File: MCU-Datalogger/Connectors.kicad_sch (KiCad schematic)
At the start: 4 parts, among them J1 Conn_01x04_Pin, J2 Conn_01x04_Pin, J3 Conn_01x09_Pin, J4 Conn_02x03_Odd_Even

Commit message: Associate footprints with symbols
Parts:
- J1, J2: footprint (none) -> Connector_PinHeader_2.54mm:PinHeader_1x04_P2.54mm_Vertical
- J3: footprint (none) -> Connector_PinHeader_2.54mm:PinHeader_1x09_P2.54mm_Vertical
- J4: footprint (none) -> Connector_PinHeader_2.54mm:PinHeader_2x03_P2.54mm_Vertical
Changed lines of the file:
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@@
       (effects (font (size 1.27 1.27)))
     )
-    (property "Footprint" "" (at 143.51 86.36 0)
+    (property "Footprint" "Connector_PinHeader_2.54mm:PinHeader_1x04_P2.54mm_Vertical" (at 143.51 86.36 0)
       (effects (font (size 1.27 1.27)) hide)
     )
@@
       (effects (font (size 1.27 1.27)))
     )
-    (property "Footprint" "" (at 149.86 120.65 0)
+    (property "Footprint" "Connector_PinHeader_2.54mm:PinHeader_2x03_P2.54mm_Vertical" (at 149.86 120.65 0)
       (effects (font (size 1.27 1.27)) hide)
     )
@@
       (effects (font (size 1.27 1.27)))
     )
-    (property "Footprint" "" (at 121.92 120.65 0)
+    (property "Footprint" "Connector_PinHeader_2.54mm:PinHeader_1x09_P2.54mm_Vertical" (at 121.92 120.65 0)
       (effects (font (size 1.27 1.27)) hide)
     )
@@
       (effects (font (size 1.27 1.27)))
     )
-    (property "Footprint" "" (at 121.92 86.36 0)
+    (property "Footprint" "Connector_PinHeader_2.54mm:PinHeader_1x04_P2.54mm_Vertical" (at 121.92 86.36 0)
       (effects (font (size 1.27 1.27)) hide)
     )

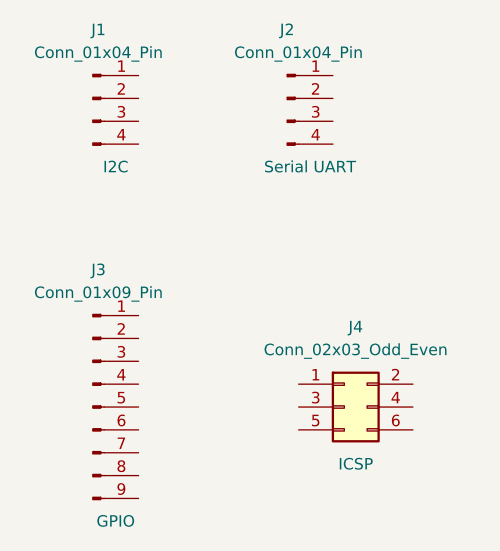
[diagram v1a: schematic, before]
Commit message: Wriring the second scheet
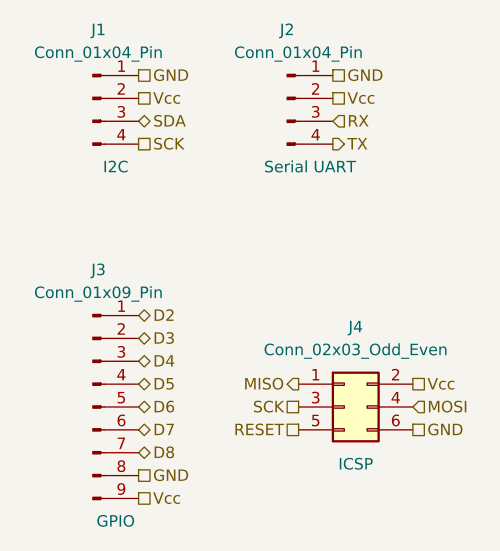
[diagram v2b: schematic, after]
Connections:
- net GND: now reaches J2.1 (Pin_1)
- net GND: now also J1.1 (Pin_1), J3.8 (Pin_8), J4.6 (Pin_6)
- net Vcc: now reaches J2.2 (Pin_2)
- net Vcc: now also J1.2 (Pin_2), J3.9 (Pin_9), J4.2 (Pin_2)
- net RX: now reaches J2.3 (Pin_3)
- net TX: now reaches J2.4 (Pin_4)
- net MISO: now reaches J4.1 (Pin_1)
- net SCK: now reaches J4.3 (Pin_3)
- net SCK: now also J1.4 (Pin_4)
- net MOSI: now reaches J4.4 (Pin_4)
- net RESET: now reaches J4.5 (Pin_5)
- net D2: now reaches J3.1 (Pin_1)
- net D3: now reaches J3.2 (Pin_2)
- net D4: now reaches J3.3 (Pin_3)
- net D5: now reaches J3.4 (Pin_4)
- net D6: now reaches J3.5 (Pin_5)
- net D7: now reaches J3.6 (Pin_6)
- net D8: now reaches J3.7 (Pin_7)
- net SDA: now reaches J1.3 (Pin_3)
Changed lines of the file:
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@@
 (kicad_sch (version 20230121) (generator eeschema)
   (paper "A4")
+  (hierarchical_label "GND" (shape passive) (at 157.48 123.19 0) (fields_autoplaced)
+    (effects (font (size 1.27 1.27)) (justify left))
+  )
+  (hierarchical_label "MISO" (shape output) (at 144.78 118.11 180) (fields_autoplaced)
+    (effects (font (size 1.27 1.27)) (justify right))
+  )
+  (hierarchical_label "SDA" (shape bidirectional) (at 127 88.9 0) (fields_autoplaced)
+    (effects (font (size 1.27 1.27)) (justify left))
+  )
+  (hierarchical_label "D2" (shape bidirectional) (at 127 110.49 0) (fields_autoplaced)
+    (effects (font (size 1.27 1.27)) (justify left))
+  )
+  (hierarchical_label "D8" (shape bidirectional) (at 127 125.73 0) (fields_autoplaced)
+    (effects (font (size 1.27 1.27)) (justify left))
+  )
+  (hierarchical_label "Vcc" (shape passive) (at 157.48 118.11 0) (fields_autoplaced)
+    (effects (font (size 1.27 1.27)) (justify left))
+  )
+  (hierarchical_label "Vcc" (shape passive) (at 127 130.81 0) (fields_autoplaced)
+    (effects (font (size 1.27 1.27)) (justify left))
+  )
+  (hierarchical_label "SCK" (shape passive) (at 144.78 120.65 180) (fields_autoplaced)
+    (effects (font (size 1.27 1.27)) (justify right))
+  )
+  (hierarchical_label "D7" (shape bidirectional) (at 127 123.19 0) (fields_autoplaced)
+    (effects (font (size 1.27 1.27)) (justify left))
+  )
+  (hierarchical_label "Vcc" (shape passive) (at 148.59 86.36 0) (fields_autoplaced)
+    (effects (font (size 1.27 1.27)) (justify left))
+  )
+  (hierarchical_label "TX" (shape output) (at 148.59 91.44 0) (fields_autoplaced)
+    (effects (font (size 1.27 1.27)) (justify left))
+  )
+  (hierarchical_label "D6" (shape bidirectional) (at 127 120.65 0) (fields_autoplaced)
+    (effects (font (size 1.27 1.27)) (justify left))
+  )
+  (hierarchical_label "GND" (shape passive) (at 148.59 83.82 0) (fields_autoplaced)
+    (effects (font (size 1.27 1.27)) (justify left))
+  )
+  (hierarchical_label "Vcc" (shape passive) (at 127 86.36 0) (fields_autoplaced)
+    (effects (font (size 1.27 1.27)) (justify left))
+  )
+  (hierarchical_label "GND" (shape passive) (at 127 128.27 0) (fields_autoplaced)
+    (effects (font (size 1.27 1.27)) (justify left))
+  )
+  (hierarchical_label "D5" (shape bidirectional) (at 127 118.11 0) (fields_autoplaced)
+    (effects (font (size 1.27 1.27)) (justify left))
+  )
+  (hierarchical_label "RESET" (shape passive) (at 144.78 123.19 180) (fields_autoplaced)
+    (effects (font (size 1.27 1.27)) (justify right))
+  )
+  (hierarchical_label "D3" (shape bidirectional) (at 127 113.03 0) (fields_autoplaced)
+    (effects (font (size 1.27 1.27)) (justify left))
+  )
+  (hierarchical_label "GND" (shape passive) (at 127 83.82 0) (fields_autoplaced)
+    (effects (font (size 1.27 1.27)) (justify left))
+  )
+  (hierarchical_label "SCK" (shape passive) (at 127 91.44 0) (fields_autoplaced)
+    (effects (font (size 1.27 1.27)) (justify left))
+  )
+  (hierarchical_label "MOSI" (shape input) (at 157.48 120.65 0) (fields_autoplaced)
+    (effects (font (size 1.27 1.27)) (justify left))
+  )
+  (hierarchical_label "D4" (shape bidirectional) (at 127 115.57 0) (fields_autoplaced)
+    (effects (font (size 1.27 1.27)) (justify left))
+  )
+  (hierarchical_label "RX" (shape input) (at 148.59 88.9 0) (fields_autoplaced)
+    (effects (font (size 1.27 1.27)) (justify left))
+  )
   (symbol (lib_id "Connector:Conn_01x04_Pin") (at 143.51 86.36 0) (unit 1)
     (in_bom yes) (on_board yes) (dnp no)

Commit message: modified SCL to SCK Label because of wrong pin was choosen
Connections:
- net SCK: no longer J1.4 (Pin_4)
- new net SCL: J1.4 (Pin_4)
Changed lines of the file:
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@@
     (effects (font (size 1.27 1.27)) (justify left))
   )
-  (hierarchical_label "SCK" (shape passive) (at 127 91.44 0) (fields_autoplaced)
+  (hierarchical_label "SCL" (shape passive) (at 127 91.44 0) (fields_autoplaced)
     (effects (font (size 1.27 1.27)) (justify left))
   )
